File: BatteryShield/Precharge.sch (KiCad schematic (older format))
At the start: 6 parts

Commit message: All footprints added for gen 1 battery board
Woot. Layout soon!!!
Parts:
- removed R?: 1k, symbol R
- added R?: 1k, Resistors_SMD:R_0603, symbol R
- D?: footprint (none) -> Diodes_SMD:D_SOD-323F
- R?: footprint TO-263-2 -> TO_SOT_Packages_SMD:TO-263-2
- R?: footprint (none) -> Resistors_SMD:R_0603
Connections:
- net GND: now also R?.2
- net at D?.2 (A), K?.5: now also R?.1
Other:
- note added: "NOTES:\n-DUE TO HEAT CONSUMTION OF RESISTOR PRECHARGE PARTS \nSHOULD NOT BE ORDERED. \n-IF NECESSARY THIS DESIGN CAN BE EXPLORED FUTHER IN THE FUTURE"
- note removed: "NOTES:\n-10 OHM RESISTOR NEEDS TO BE POWER RATED\n-UNDER VACCUM CONDITIONS 10 OHM RESISTOR WOULD SINK A FAIR AMOUNT OF POWER, THIS NEEDS TO TAKEN INTO CONSIDERATION\n-INSTEAD OF RESISTOR, CURRENT LIMITING INDUCTOR COULD BE USED (NO HEAT DISSAPATION)\n\n"
- moved on the sheet: D?, K?, Q?, R?
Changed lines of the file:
@@
 Comment4 ""
 $EndDescr
-Text GLabel 3500 2450 0    60   Input ~ 0
+Text GLabel 5250 4250 0    60   Input ~ 0
 V_BATT37_PC
 $Comp
 L R R?
 U 1 1 5B0F060B
-P 4550 2450
-F 0 "R?" V 4630 2450 50  0000 C CNN
-F 1 "10" V 4550 2450 50  0000 C CNN
-F 2 "TO-263-2" V 4480 2450 50  0001 C CNN
-F 3 "http://www.caddock.com/Online_catalog/Mrktg_Lit/MP725.pdf" H 4550 2450 50  0001 C CNN
-	1    4550 2450
+P 6300 4250
+F 0 "R?" V 6380 4250 50  0000 C CNN
+F 1 "10" V 6300 4250 50  0000 C CNN
+F 2 "TO_SOT_Packages_SMD:TO-263-2" V 6230 4250 50  0001 C CNN
+F 3 "http://www.caddock.com/Online_catalog/Mrktg_Lit/MP725.pdf" H 6300 4250 50  0001 C CNN
+	1    6300 4250
 	0    1    1    0
 $EndComp
@@
 L G5Q-1A K?
 U 1 1 5B0F0DA1
-P 4350 1450
-F 0 "K?" V 4100 1450 50  0000 L CNN
-F 1 "G5LE-14 DC3" V 4900 1400 50  0000 L CNN
-F 2 "Relays_THT:Relay_SPST-NO_OMRON-G5Q" H 4900 1600 50  0001 L CNN
-F 3 "" H 5450 1150 50  0001 C CNN
-	1    4350 1450
+P 6100 3250
+F 0 "K?" V 5850 3250 50  0000 L CNN
+F 1 "G5LE-14 DC3" V 6650 3200 50  0000 L CNN
+F 2 "Relays_THT:Relay_SPST-NO_OMRON-G5Q" H 6650 3400 50  0001 L CNN
+F 3 "" H 7200 2950 50  0001 C CNN
+	1    6100 3250
 	0    1    1    0
 $EndComp
-Text GLabel 5750 2450 2    60   Input ~ 0
+Text GLabel 7500 4250 2    60   Input ~ 0
 V_BATT37
 $Comp
-L GND #PWR?
+L GND #PWR08
 U 1 1 5B0F1AA8
-P 5450 1650
-F 0 "#PWR?" H 5450 1400 50  0001 C CNN
-F 1 "GND" H 5450 1500 50  0000 C CNN
-F 2 "" H 5450 1650 50  0001 C CNN
-F 3 "" H 5450 1650 50  0001 C CNN
-	1    5450 1650
+P 7200 3450
+F 0 "#PWR08" H 7200 3200 50  0001 C CNN
+F 1 "GND" H 7200 3300 50  0000 C CNN
+F 2 "" H 7200 3450 50  0001 C CNN
+F 3 "" H 7200 3450 50  0001 C CNN
+	1    7200 3450
 	1    0    0    -1
 $EndComp
-Text GLabel 2050 1800 0    60   Input ~ 0
+Text GLabel 3800 3600 0    60   Input ~ 0
 PRECHARGE_N
 $Comp
-L GND #PWR?
+L GND #PWR09
 U 1 1 5B0F1D11
-P 2650 2250
-F 0 "#PWR?" H 2650 2000 50  0001 C CNN
-F 1 "GND" H 2650 2100 50  0000 C CNN
-F 2 "" H 2650 2250 50  0001 C CNN
-F 3 "" H 2650 2250 50  0001 C CNN
-	1    2650 2250
+P 4400 4050
+F 0 "#PWR09" H 4400 3800 50  0001 C CNN
+F 1 "GND" H 4400 3900 50  0000 C CNN
+F 2 "" H 4400 4050 50  0001 C CNN
+F 3 "" H 4400 4050 50  0001 C CNN
+	1    4400 4050
 	1    0    0    -1
 $EndComp
@@
 L R R?
 U 1 1 5B0F1D2F
-P 2650 2000
-F 0 "R?" V 2730 2000 50  0000 C CNN
-F 1 "1k" V 2650 2000 50  0000 C CNN
-F 2 "" V 2580 2000 50  0001 C CNN
-F 3 "" H 2650 2000 50  0001 C CNN
-	1    2650 2000
+P 4400 3800
+F 0 "R?" V 4480 3800 50  0000 C CNN
+F 1 "1k" V 4400 3800 50  0000 C CNN
+F 2 "Resistors_SMD:R_0603" V 4330 3800 50  0001 C CNN
+F 3 "https://industrial.panasonic.com/cdbs/www-data/pdf/RDM0000/AOA0000C307.pdf" H 4400 3800 50  0001 C CNN
+	1    4400 3800
 	-1   0    0    1
 $EndComp
@@
 L D D?
 U 1 1 5B0F22D2
-P 4550 850
-F 0 "D?" H 4550 950 50  0000 C CNN
-F 1 "D" H 4550 750 50  0000 C CNN
-F 2 "" H 4550 850 50  0001 C CNN
-F 3 "" H 4550 850 50  0001 C CNN
-	1    4550 850
+P 6300 2650
+F 0 "D?" H 6300 2750 50  0000 C CNN
+F 1 "D" H 6300 2550 50  0000 C CNN
+F 2 "Diodes_SMD:D_SOD-323F" H 6300 2650 50  0001 C CNN
+F 3 "http://www.comchiptech.com/cms/UserFiles/CDSF4148-RevD370195.pdf" H 6300 2650 50  0001 C CNN
+	1    6300 2650
 	1    0    0    -1
 $EndComp
 Wire Wire Line
-	3500 2450 4400 2450
+	5250 4250 6150 4250
 Wire Wire Line
-	4700 2450 5750 2450
+	6450 4250 7500 4250
 Wire Wire Line
-	4150 2450 4150 1850
+	5900 4250 5900 3650
 Wire Wire Line
-	4150 1850 4250 1850
-Connection ~ 4150 2450
+	5900 3650 6000 3650
+Connection ~ 5900 4250
 Wire Wire Line
-	4850 1850 5000 1850
+	6600 3650 6750 3650
 Wire Wire Line
-	5000 1850 5000 2450
-Connection ~ 5000 2450
+	6750 3650 6750 4250
+Connection ~ 6750 4250
 Wire Wire Line
-	3800 2450 3800 2000
-Connection ~ 3800 2450
+	5550 4250 5550 3800
+Connection ~ 5550 4250
 Wire Wire Line
-	3800 1600 3800 1450
+	5550 3400 5550 3250
 Wire Wire Line
-	3800 1450 4250 1450
+	5550 3250 6000 3250
 Wire Wire Line
-	5450 1450 5450 1650
+	7200 3250 7200 3450
 Wire Wire Line
-	2050 1800 3500 1800
+	3800 3600 5250 3600
 Wire Wire Line
-	2650 1850 2650 1800
-Connection ~ 2650 1800
+	4400 3650 4400 3600
+Connection ~ 4400 3600
 Wire Wire Line
-	2650 2150 2650 2250
+	4400 3950 4400 4050
 Wire Wire Line
-	4150 1450 4150 850
+	5900 3250 5900 2650
 Wire Wire Line
-	4150 850  4400 850
-Connection ~ 4150 1450
+	5900 2650 6150 2650
+Connection ~ 5900 3250
 Wire Wire Line
-	4700 850  4950 850
+	6450 2650 6700 2650
 Wire Wire Line
-	4950 850  4950 1450
-Connection ~ 4950 1450
-$Comp
-L R R?
-U 1 1 5B103E03
-P 5200 1450
-F 0 "R?" V 5280 1450 50  0000 C CNN
-F 1 "1k" V 5200 1450 50  0000 C CNN
-F 2 "" V 5130 1450 50  0001 C CNN
-F 3 "" H 5200 1450 50  0001 C CNN
-	1    5200 1450
-	0    -1   -1   0
-$EndComp
+	6700 2650 6700 3250
+Connection ~ 6700 3250
 Wire Wire Line
-	4850 1450 5050 1450
+	6600 3250 6800 3250
 Wire Wire Line
-	5350 1450 5450 1450
-Text Notes 1250 2950 0    60   ~ 0
-NOTES:\n-10 OHM RESISTOR NEEDS TO BE POWER RATED\n-UNDER VACCUM CONDITIONS 10 OHM RESISTOR WOULD SINK A FAIR AMOUNT OF POWER, THIS NEEDS TO TAKEN INTO CONSIDERATION\n-INSTEAD OF RESISTOR, CURRENT LIMITING INDUCTOR COULD BE USED (NO HEAT DISSAPATION)\n\n
-Text GLabel 3450 5700 0    60   Input ~ 0
-V_BATT37_PC
-Text GLabel 7150 5600 2    60   Input ~ 0
-V_BATT37
+	7100 3250 7200 3250
+Text Notes 4700 4850 0    60   ~ 0
+NOTES:\n-DUE TO HEAT CONSUMTION OF RESISTOR PRECHARGE PARTS \nSHOULD NOT BE ORDERED. \n-IF NECESSARY THIS DESIGN CAN BE EXPLORED FUTHER IN THE FUTURE
 $Comp
 L BSS138 Q?
 U 1 1 5B298E62
-P 3700 1800
-F 0 "Q?" H 3900 1875 50  0000 L CNN
-F 1 "ZVN4525G" H 3900 1800 50  0000 L CNN
-F 2 "TO_SOT_Packages_SMD:SOT-23" H 3900 1725 50  0001 L CIN
-F 3 "" H 3700 1800 50  0001 L CNN
-	1    3700 1800
+P 5450 3600
+F 0 "Q?" H 5650 3675 50  0000 L CNN
+F 1 "ZVN4525G" H 5650 3600 50  0000 L CNN
+F 2 "TO_SOT_Packages_SMD:SOT-23" H 5650 3525 50  0001 L CIN
+F 3 "" H 5450 3600 50  0001 L CNN
+	1    5450 3600
 	1    0    0    -1
 $EndComp
+$Comp
+L R R?
+U 1 1 5B2A2B88
+P 6950 3250
+F 0 "R?" V 7030 3250 50  0000 C CNN
+F 1 "1k" V 6950 3250 50  0000 C CNN
+F 2 "Resistors_SMD:R_0603" V 6880 3250 50  0001 C CNN
+F 3 "https://industrial.panasonic.com/cdbs/www-data/pdf/RDM0000/AOA0000C307.pdf" H 6950 3250 50  0001 C CNN
+	1    6950 3250
+	0    -1   -1   0
+$EndComp
 $EndSCHEMATC

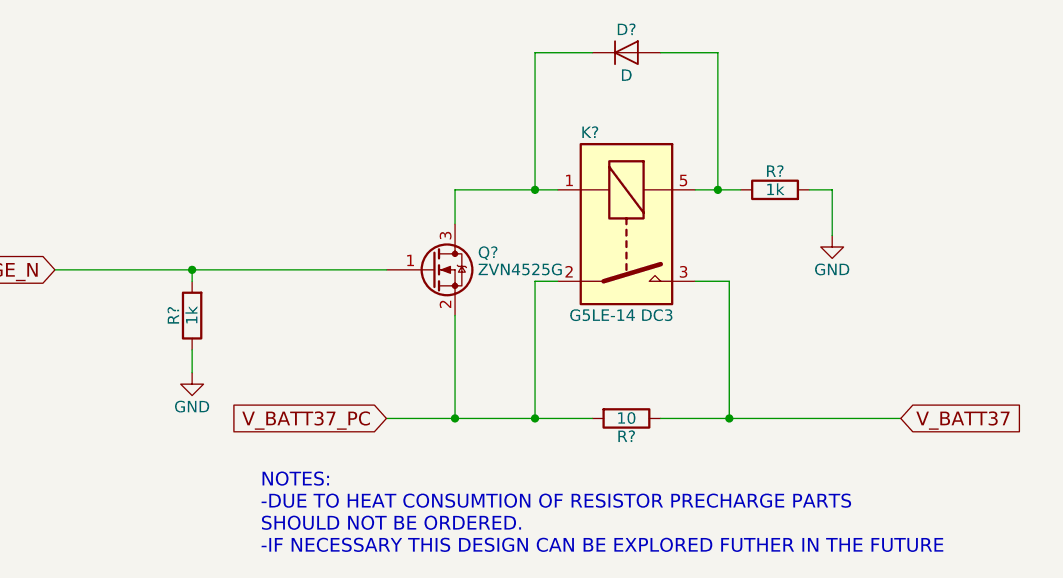
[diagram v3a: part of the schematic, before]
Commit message: Did V.1 of layout; removed old circuits
gosh I need to do schoolwork
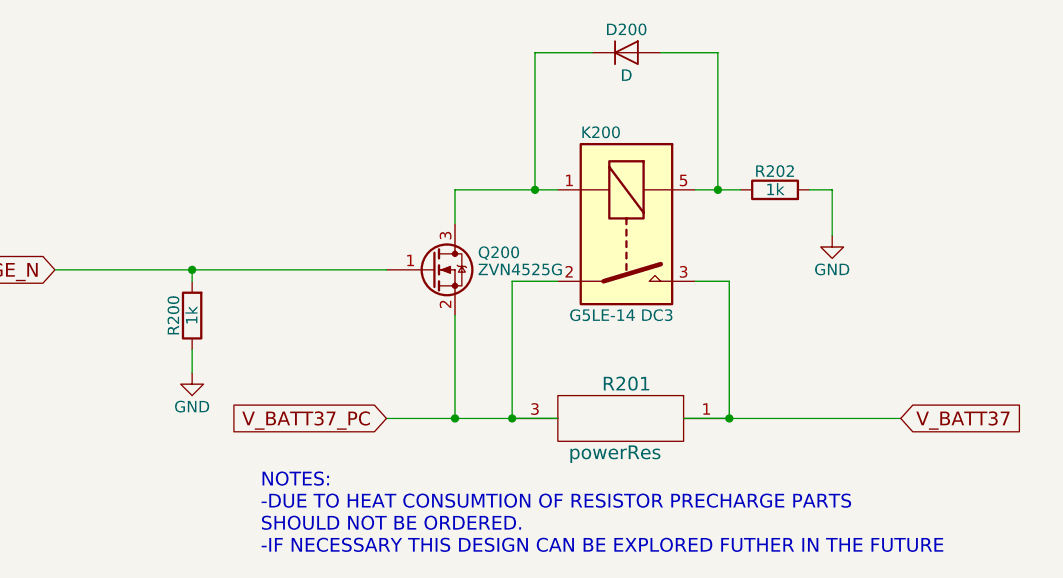
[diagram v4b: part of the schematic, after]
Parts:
- removed R?: 10, TO_SOT_Packages_SMD:TO-263-2, symbol R
- added R201: powerRes, TO_SOT_Packages_SMD:TO-263-2, symbol powerRes
- K200: renamed from K?; footprint Relays_THT:Relay_SPST-NO_OMRON-G5Q -> Relays_THT:Relay_SPDT_OMRON-G5Q
- gave numbers to parts that had none: 4
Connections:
- net V_BATT37: now also R201.1
- net V_BATT37_PC: now also R201.3
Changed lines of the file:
@@
 LIBS:LTC4151IMS-1-PBF
 LIBS:sensors
+LIBS:powerRes
 LIBS:Battery_Shield-cache
 EELAYER 25 0
@@
 $Descr A4 11693 8268
 encoding utf-8
-Sheet 4 12
+Sheet 3 8
 Title ""
 Date ""
@@
 V_BATT37_PC
 $Comp
-L R R?
-U 1 1 5B0F060B
-P 6300 4250
-F 0 "R?" V 6380 4250 50  0000 C CNN
-F 1 "10" V 6300 4250 50  0000 C CNN
-F 2 "TO_SOT_Packages_SMD:TO-263-2" V 6230 4250 50  0001 C CNN
-F 3 "http://www.caddock.com/Online_catalog/Mrktg_Lit/MP725.pdf" H 6300 4250 50  0001 C CNN
-	1    6300 4250
-	0    1    1    0
-$EndComp
-$Comp
-L G5Q-1A K?
+L G5Q-1A K200
 U 1 1 5B0F0DA1
 P 6100 3250
-F 0 "K?" V 5850 3250 50  0000 L CNN
+F 0 "K200" V 5850 3250 50  0000 L CNN
 F 1 "G5LE-14 DC3" V 6650 3200 50  0000 L CNN
-F 2 "Relays_THT:Relay_SPST-NO_OMRON-G5Q" H 6650 3400 50  0001 L CNN
+F 2 "Relays_THT:Relay_SPDT_OMRON-G5Q" H 6650 3400 50  0001 L CNN
 F 3 "" H 7200 2950 50  0001 C CNN
 	1    6100 3250
@@
 V_BATT37
 $Comp
-L GND #PWR08
+L GND #PWR04
 U 1 1 5B0F1AA8
 P 7200 3450
-F 0 "#PWR08" H 7200 3200 50  0001 C CNN
+F 0 "#PWR04" H 7200 3200 50  0001 C CNN
 F 1 "GND" H 7200 3300 50  0000 C CNN
 F 2 "" H 7200 3450 50  0001 C CNN
@@
 PRECHARGE_N
 $Comp
-L GND #PWR09
+L GND #PWR05
 U 1 1 5B0F1D11
 P 4400 4050
-F 0 "#PWR09" H 4400 3800 50  0001 C CNN
+F 0 "#PWR05" H 4400 3800 50  0001 C CNN
 F 1 "GND" H 4400 3900 50  0000 C CNN
 F 2 "" H 4400 4050 50  0001 C CNN
@@
 $EndComp
 $Comp
-L R R?
+L R R200
 U 1 1 5B0F1D2F
 P 4400 3800
-F 0 "R?" V 4480 3800 50  0000 C CNN
+F 0 "R200" V 4480 3800 50  0000 C CNN
 F 1 "1k" V 4400 3800 50  0000 C CNN
 F 2 "Resistors_SMD:R_0603" V 4330 3800 50  0001 C CNN
@@
 $EndComp
 $Comp
-L D D?
+L D D200
 U 1 1 5B0F22D2
 P 6300 2650
-F 0 "D?" H 6300 2750 50  0000 C CNN
+F 0 "D200" H 6300 2750 50  0000 C CNN
 F 1 "D" H 6300 2550 50  0000 C CNN
 F 2 "Diodes_SMD:D_SOD-323F" H 6300 2650 50  0001 C CNN
@@
 $EndComp
 Wire Wire Line
-	5250 4250 6150 4250
+	5250 4250 6000 4250
 Wire Wire Line
-	6450 4250 7500 4250
-Wire Wire Line
-	5900 4250 5900 3650
-Wire Wire Line
-	5900 3650 6000 3650
-Connection ~ 5900 4250
+	5800 3650 6000 3650
 Wire Wire Line
 	6600 3650 6750 3650
-Wire Wire Line
-	6750 3650 6750 4250
-Connection ~ 6750 4250
 Wire Wire Line
 	5550 4250 5550 3800
@@
 NOTES:\n-DUE TO HEAT CONSUMTION OF RESISTOR PRECHARGE PARTS \nSHOULD NOT BE ORDERED. \n-IF NECESSARY THIS DESIGN CAN BE EXPLORED FUTHER IN THE FUTURE
 $Comp
-L BSS138 Q?
+L BSS138 Q200
 U 1 1 5B298E62
 P 5450 3600
-F 0 "Q?" H 5650 3675 50  0000 L CNN
+F 0 "Q200" H 5650 3675 50  0000 L CNN
 F 1 "ZVN4525G" H 5650 3600 50  0000 L CNN
 F 2 "TO_SOT_Packages_SMD:SOT-23" H 5650 3525 50  0001 L CIN
@@
 $EndComp
 $Comp
-L R R?
+L R R202
 U 1 1 5B2A2B88
 P 6950 3250
-F 0 "R?" V 7030 3250 50  0000 C CNN
+F 0 "R202" V 7030 3250 50  0000 C CNN
 F 1 "1k" V 6950 3250 50  0000 C CNN
 F 2 "Resistors_SMD:R_0603" V 6880 3250 50  0001 C CNN
@@
 	0    -1   -1   0
 $EndComp
+$Comp
+L powerRes R201
+U 1 1 5B2E7ED6
+P 6300 4250
+F 0 "R201" V 6150 4250 60  0000 C CNN
+F 1 "powerRes" V 6450 4200 60  0000 C CNN
+F 2 "TO_SOT_Packages_SMD:TO-263-2" H 6300 4250 60  0001 C CNN
+F 3 "http://www.caddock.com/Online_catalog/Mrktg_Lit/MP725.pdf" H 6300 4250 60  0001 C CNN
+	1    6300 4250
+	0    1    1    0
+$EndComp
+Wire Wire Line
+	6550 4250 7500 4250
+Wire Wire Line
+	6750 3650 6750 4250
+Connection ~ 6750 4250
+Wire Wire Line
+	5800 3650 5800 4250
+Connection ~ 5800 4250
 $EndSCHEMATC

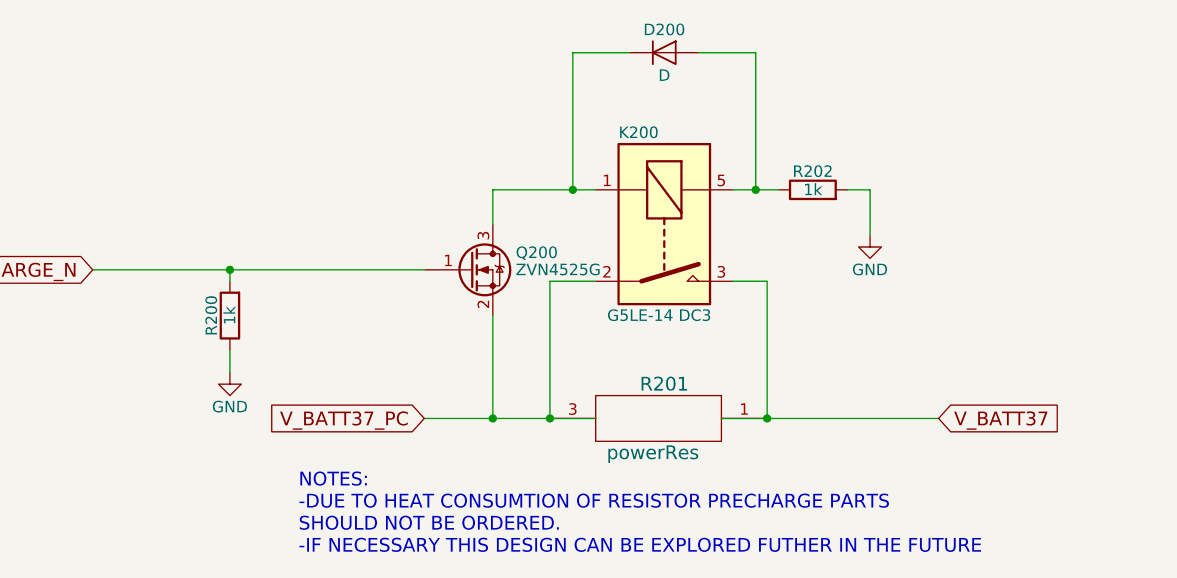
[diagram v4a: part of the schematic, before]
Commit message: fixed transistors
Fixed transistor issue with precharge circuit, added some extra optional bom modifications
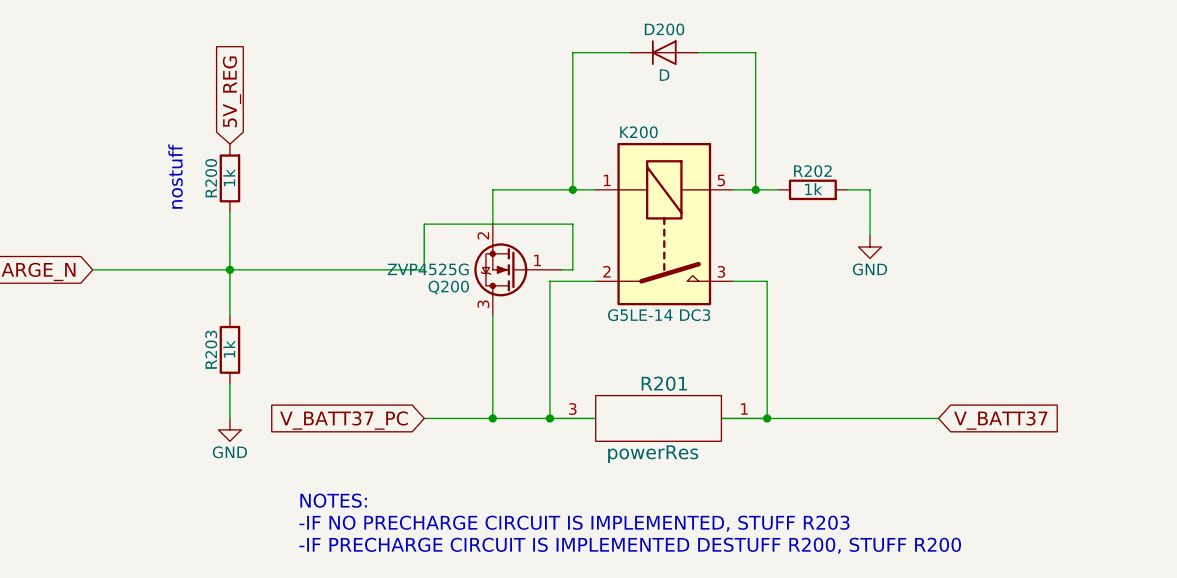
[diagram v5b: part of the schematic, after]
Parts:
- added R203: 1k, Resistors_SMD:R_0603, symbol R
- Q200: value ZVN4525G -> ZVP4525G; footprint TO_SOT_Packages_SMD:SOT-23 -> TO_SOT_Packages_SMD:SOT-223
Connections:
- net GND: now also R203.1; no longer R200.1
- net PRECHARGE_N: now also R200.1, R203.2; no longer R200.2
- net V_BATT37_PC: now also Q200.3 (D); no longer Q200.2 (S)
- net at D200.1 (K), K200.1: now also Q200.2 (S); no longer Q200.3 (D)
- new net 5V_REG: R200.2
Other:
- note added: "NOTES:\n-IF NO PRECHARGE CIRCUIT IS IMPLEMENTED, STUFF R203\n-IF PRECHARGE CIRCUIT IS IMPLEMENTED DESTUFF R200, STUFF R200\n"
- note added: "nostuff\n"
- note removed: "NOTES:\n-DUE TO HEAT CONSUMTION OF RESISTOR PRECHARGE PARTS \nSHOULD NOT BE ORDERED. \n-IF NECESSARY THIS DESIGN CAN BE EXPLORED FUTHER IN THE FUTURE"
- moved on the sheet: Q200, R200
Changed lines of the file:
@@
 PRECHARGE_N
-$Comp
-L GND #PWR05
-U 1 1 5B0F1D11
-P 4400 4050
-F 0 "#PWR05" H 4400 3800 50  0001 C CNN
-F 1 "GND" H 4400 3900 50  0000 C CNN
-F 2 "" H 4400 4050 50  0001 C CNN
-F 3 "" H 4400 4050 50  0001 C CNN
-	1    4400 4050
-	1    0    0    -1
-$EndComp
 $Comp
 L R R200
 U 1 1 5B0F1D2F
-P 4400 3800
-F 0 "R200" V 4480 3800 50  0000 C CNN
-F 1 "1k" V 4400 3800 50  0000 C CNN
-F 2 "Resistors_SMD:R_0603" V 4330 3800 50  0001 C CNN
-F 3 "https://industrial.panasonic.com/cdbs/www-data/pdf/RDM0000/AOA0000C307.pdf" H 4400 3800 50  0001 C CNN
-	1    4400 3800
+P 4400 3200
+F 0 "R200" V 4480 3200 50  0000 C CNN
+F 1 "1k" V 4400 3200 50  0000 C CNN
+F 2 "Resistors_SMD:R_0603" V 4330 3200 50  0001 C CNN
+F 3 "https://industrial.panasonic.com/cdbs/www-data/pdf/RDM0000/AOA0000C307.pdf" H 4400 3200 50  0001 C CNN
+	1    4400 3200
 	-1   0    0    1
 $EndComp
@@
 Wire Wire Line
 	3800 3600 5250 3600
-Wire Wire Line
-	4400 3650 4400 3600
 Connection ~ 4400 3600
-Wire Wire Line
-	4400 3950 4400 4050
 Wire Wire Line
 	5900 3250 5900 2650
@@
 	7100 3250 7200 3250
 Text Notes 4700 4850 0    60   ~ 0
-NOTES:\n-DUE TO HEAT CONSUMTION OF RESISTOR PRECHARGE PARTS \nSHOULD NOT BE ORDERED. \n-IF NECESSARY THIS DESIGN CAN BE EXPLORED FUTHER IN THE FUTURE
+NOTES:\n-IF NO PRECHARGE CIRCUIT IS IMPLEMENTED, STUFF R203\n-IF PRECHARGE CIRCUIT IS IMPLEMENTED DESTUFF R200, STUFF R200\n
 $Comp
 L BSS138 Q200
 U 1 1 5B298E62
-P 5450 3600
-F 0 "Q200" H 5650 3675 50  0000 L CNN
-F 1 "ZVN4525G" H 5650 3600 50  0000 L CNN
-F 2 "TO_SOT_Packages_SMD:SOT-23" H 5650 3525 50  0001 L CIN
-F 3 "" H 5450 3600 50  0001 L CNN
-	1    5450 3600
-	1    0    0    -1
+P 5650 3600
+F 0 "Q200" H 5850 3675 50  0000 L CNN
+F 1 "ZVP4525G" H 5850 3600 50  0000 L CNN
+F 2 "TO_SOT_Packages_SMD:SOT-223" H 5850 3525 50  0001 L CIN
+F 3 "" H 5650 3600 50  0001 L CNN
+	1    5650 3600
+	-1   0    0    1
 $EndComp
 $Comp
@@
 	5800 3650 5800 4250
 Connection ~ 5800 4250
+Wire Wire Line
+	5900 3600 5850 3600
+Wire Wire Line
+	5900 3600 5900 3400
+Wire Wire Line
+	5900 3400 5250 3400
+Wire Wire Line
+	5250 3400 5250 3600
+Wire Wire Line
+	4400 3350 4400 3800
+Text GLabel 4400 3050 1    60   Input ~ 0
+5V_REG
+$Comp
+L R R203
+U 1 1 5B34256E
+P 4400 3950
+F 0 "R203" V 4480 3950 50  0000 C CNN
+F 1 "1k" V 4400 3950 50  0000 C CNN
+F 2 "Resistors_SMD:R_0603" V 4330 3950 50  0001 C CNN
+F 3 "https://industrial.panasonic.com/cdbs/www-data/pdf/RDM0000/AOA0000C307.pdf" H 4400 3950 50  0001 C CNN
+	1    4400 3950
+	-1   0    0    1
+$EndComp
+$Comp
+L GND #PWR05
+U 1 1 5B342729
+P 4400 4250
+F 0 "#PWR05" H 4400 4000 50  0001 C CNN
+F 1 "GND" H 4400 4100 50  0000 C CNN
+F 2 "" H 4400 4250 50  0001 C CNN
+F 3 "" H 4400 4250 50  0001 C CNN
+	1    4400 4250
+	1    0    0    -1
+$EndComp
+Wire Wire Line
+	4400 4250 4400 4100
+Text Notes 4200 3350 1    60   ~ 0
+nostuff\n
 $EndSCHEMATC

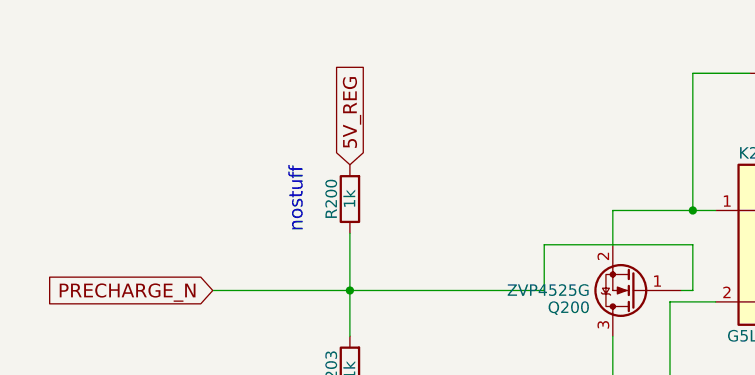
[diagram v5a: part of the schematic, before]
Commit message: Redid Layout for battery shield. Now V2
Way cleaner, no trace loops and the ground plane is MUCH cleaner.
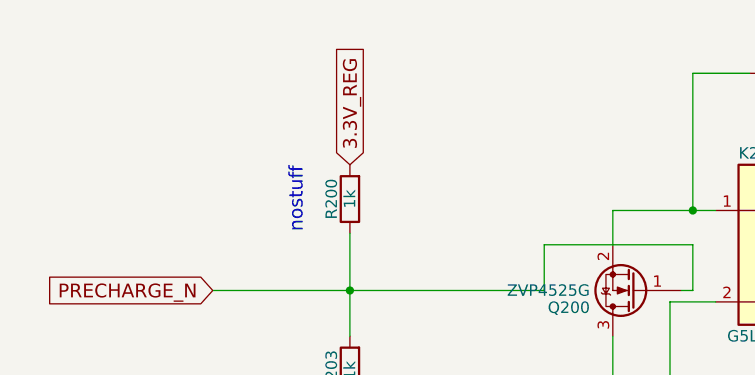
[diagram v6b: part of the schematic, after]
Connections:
- net 5V_REG renamed 3.3V_REG
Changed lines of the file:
@@
 	4400 3350 4400 3800
 Text GLabel 4400 3050 1    60   Input ~ 0
-5V_REG
+3.3V_REG
 $Comp
 L R R203
